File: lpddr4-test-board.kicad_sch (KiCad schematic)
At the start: 2 parts

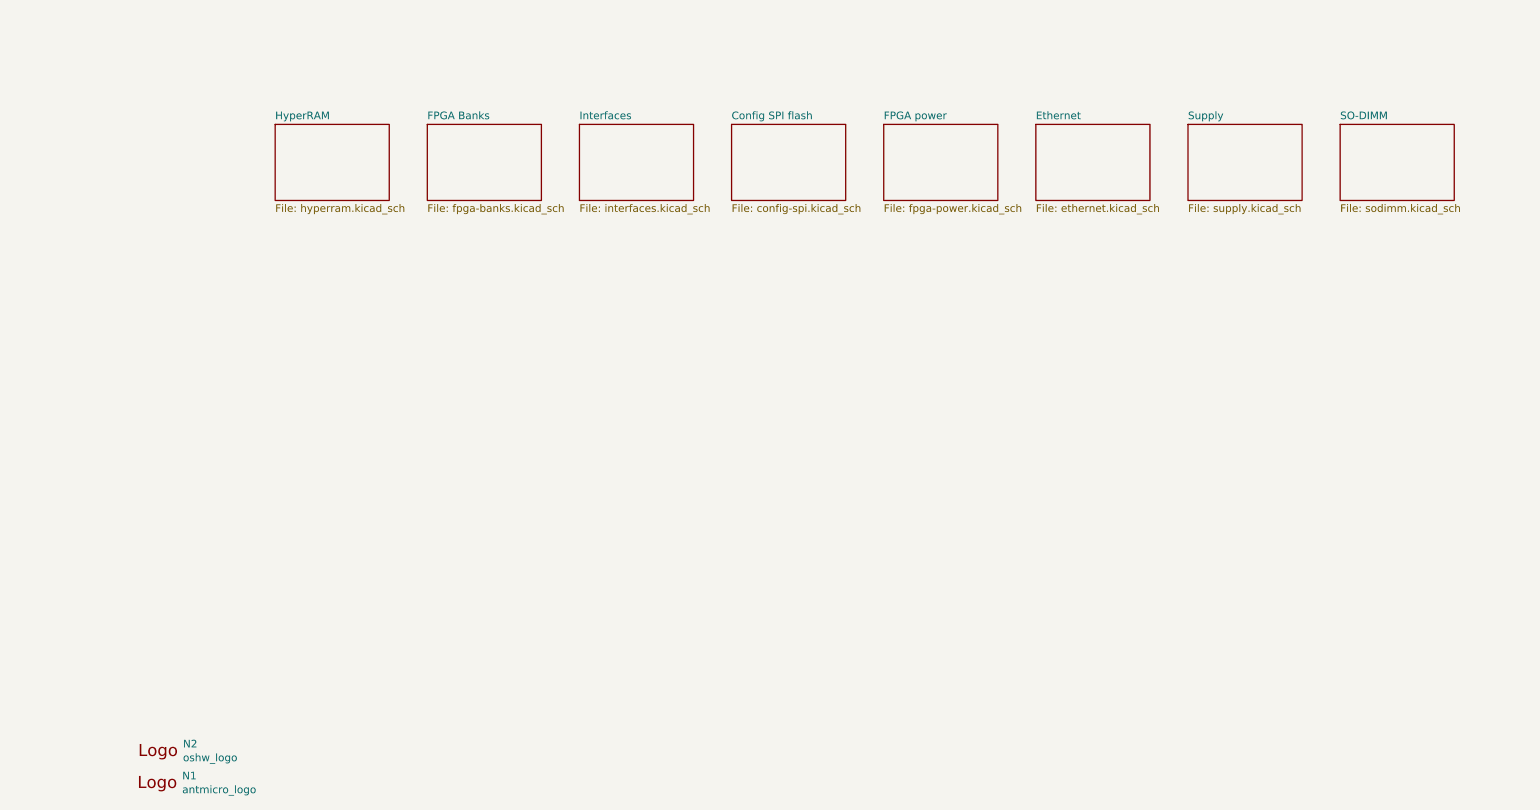
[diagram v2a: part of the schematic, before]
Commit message: Introduce standardized components
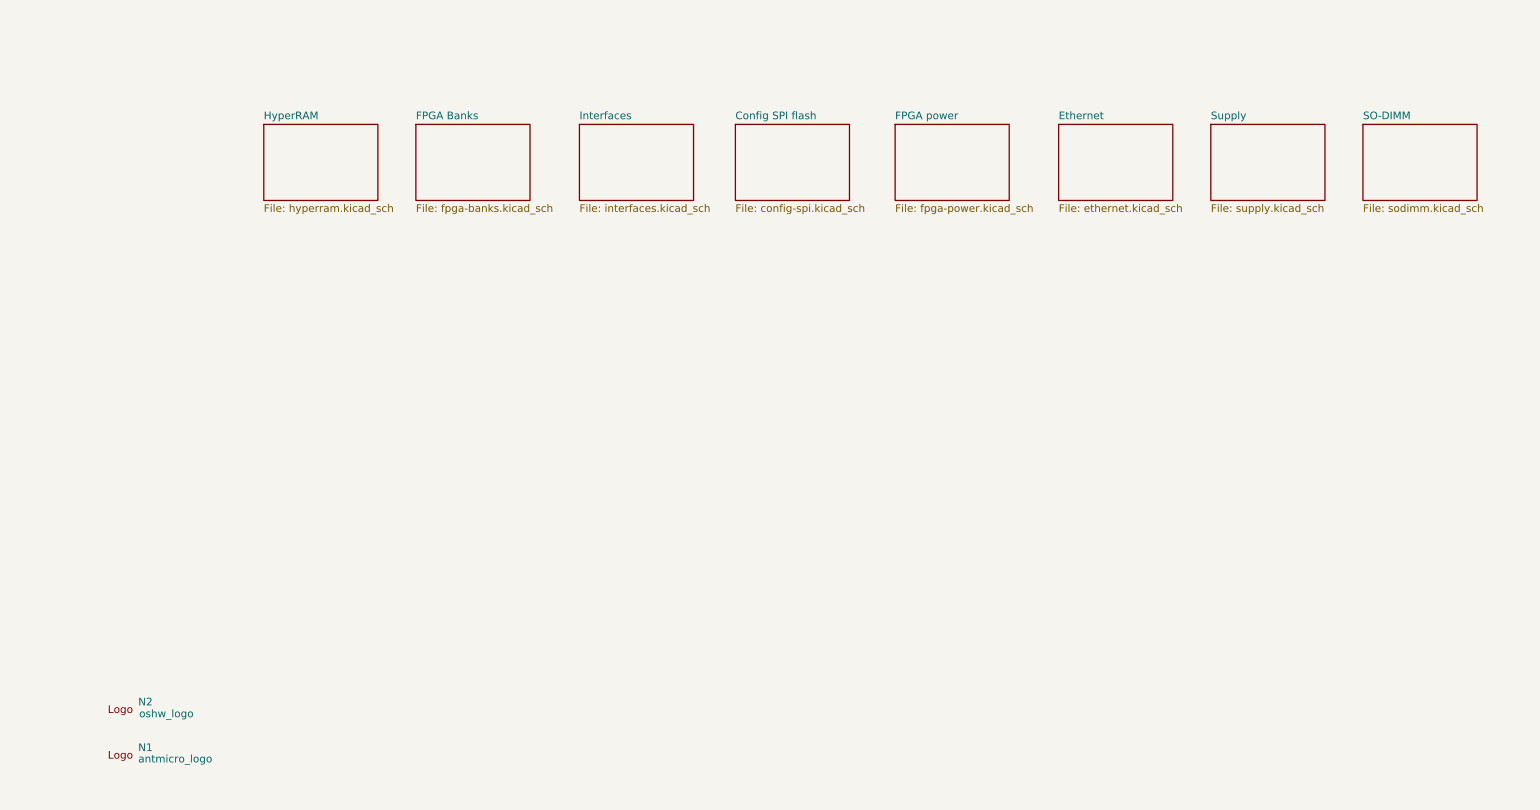
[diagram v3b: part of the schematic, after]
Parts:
- N1, N2: Author (none) -> Antmicro; License (none) -> Apache-2.0
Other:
- moved on the sheet: N1, N2

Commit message: [#55158] components update
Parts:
- N1: footprint lpddr4-test-board-footprints:antmicro-logo_scaled_20mm -> lpddr4-test-board-footprints:antmicro-logo
